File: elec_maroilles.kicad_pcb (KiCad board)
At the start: 2 copper layers, 100 x 90 mm, 88 parts, among them J1 USB_A vert., J2 USB_A vert., J3 Pico5, J4 Dynamixel-3, J5 Dynamixel-3, J6 Pico5, J7 Pico5, J8 Dynamixel-4, J9 Dynamixel-4, Q1 MMBT3906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

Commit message: [update] Positionning v1
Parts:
- removed D3: SP0503BAHT, Package_TO_SOT_SMD:SOT-143
- removed J2: USB_A vert., Library_Pollen:Amphenol_LUSBA11100
- removed TP2, TP4: TestPoint, TestPoint:TestPoint_Pad_D1.0mm
- added J10: PicoBlade 5, Connector_Molex:Molex_PicoBlade_53398-0571_1x05-1MP_P1.25mm_Vertical, F.Cu at (176.6, 63.5)
- added J11: PicoBlade 5, Connector_Molex:Molex_PicoBlade_53398-0571_1x05-1MP_P1.25mm_Vertical, F.Cu at (176.6, 70.5)
- added J12: PicoBlade 5, Connector_Molex:Molex_PicoBlade_53398-0571_1x05-1MP_P1.25mm_Vertical, F.Cu at (176.6, 77.5)
- added R23: DNP - 0R, Resistor_SMD:R_0402_1005Metric, F.Cu at (138.0, 75.8)
- added R24: DNP - 0R, Resistor_SMD:R_0402_1005Metric, F.Cu at (195.9, 62.7)
- added R25: 0R, Resistor_SMD:R_0402_1005Metric, F.Cu at (196.8, 60.9)
- D11, D13, D14, D9: value B5819WS -> DNP - B5819WS
- J4, J5: value Dynamixel-3 -> DNP - Dynamixel-3
- J8, J9: value Dynamixel-4 -> DNP - Dynamixel-4
- moved FID3 117.1 mm to (226.8, 69.4)
- moved H7 83.1 mm to (226.8, 78.4)
- moved J7 81.1 mm to (128.4, 61.1), turned to 180 degrees
- moved D14 74.8 mm to (129.2, 65.8), turned to 90 degrees
- moved D13 73.9 mm to (126.2, 65.8), turned to 90 degrees
- moved FID1 71.6 mm to (89.8, 59.4)
- moved J6 68.4 mm to (214.9, 62.3), turned to 180 degrees
- moved D15 67.4 mm to (214.5, 67.2), turned to -90 degrees
- moved D16 63.2 mm to (211.5, 67.2), turned to -90 degrees
- moved H3 61.7 mm to (99.4, 59.5)
- moved H2 61.2 mm to (92.2, 61.3)
- moved H6 54.4 mm to (226.8, 61.4)
- moved J8 51.5 mm to (155.2, 78.1)
- moved J9 51.5 mm to (161.0, 78.1)
- moved C11 50.5 mm to (133.1, 66.2)
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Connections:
- Q1 pad 3: /Dynamixel TTL/Dynamixel_dir -> Net-(Q1-C)
- Q2 pad 3: /Dynamixel RS485/Dynamixel_dir -> Net-(Q2-C)
- R12 pad 2: /Dynamixel TTL/Dynamixel_dir -> Net-(Q1-C)
- R18 pad 2: /Dynamixel RS485/Dynamixel_dir -> Net-(Q2-C)
- R19 pad 1: /Dynamixel RS485/Dynamixel_dir -> Net-(Q2-C)
- R19 pad 2: Net-(U7-DE) -> /Dynamixel RS485/Dynamixel_dir
- U1 pad 12: /Dynamixel TTL/USB_DynM -> /Dynamixel TTL/USB_DynP
- U3 pad 7: /Dynamixel TTL/USB_DynM -> /Dynamixel TTL/USB_DynP
- U7 pad 2: Net-(U7-DE) -> /Dynamixel RS485/Dynamixel_dir
- U7 pad 3: Net-(U7-DE) -> /Dynamixel RS485/Dynamixel_dir
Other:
- board size 100 x 90 mm -> 150 x 25 mm

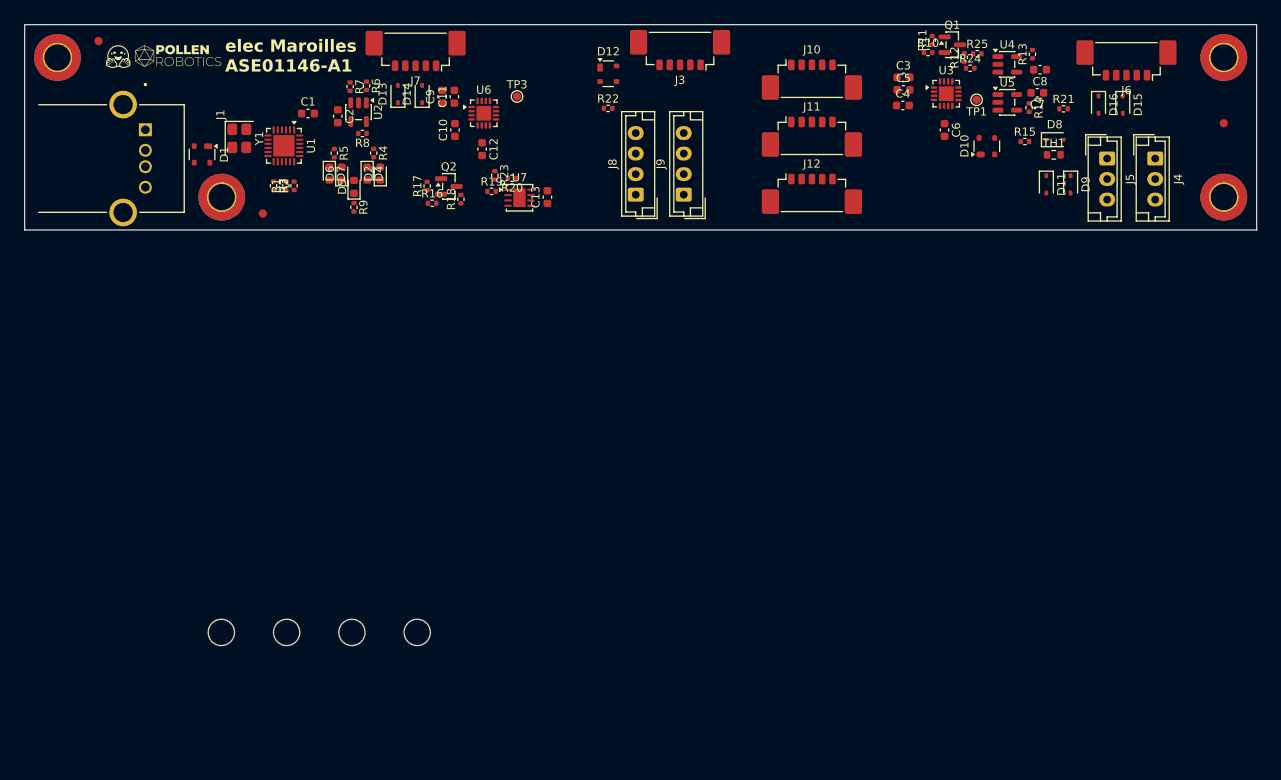
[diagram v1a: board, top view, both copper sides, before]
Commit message: [update] Better positionning.
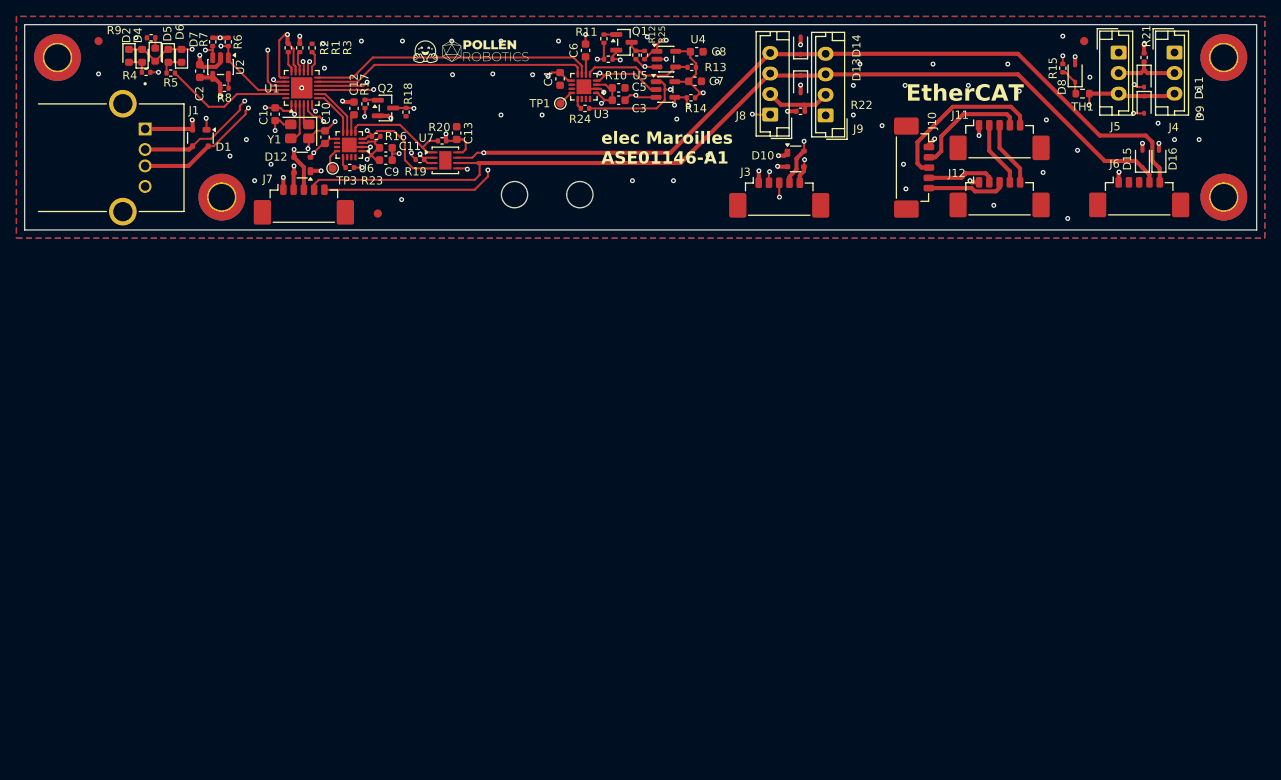
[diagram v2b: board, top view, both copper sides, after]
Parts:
- removed H12, H13: MountingHole_Pad, MountingHole:MountingHole_3.2mm_M3
- moved H10 64.2 mm to (140.4, 78.1)
- moved H11 64.2 mm to (148.4, 78.1)
- moved TP1 50.7 mm to (146.0, 67.0), turned to 0 degrees
- moved D13 49.0 mm to (175.3, 64.7), turned to -90 degrees
- moved R24 47.2 mm to (149.0, 67.6)
- moved D14 46.5 mm to (175.3, 60.0)
- moved C6 44.8 mm to (149.1, 60.5), turned to 90 degrees
- moved U3 44.1 mm to (148.9, 65.0), turned to 180 degrees
- moved C4 41.9 mm to (146.0, 64.0), turned to 90 degrees
- moved C8 41.9 mm to (162.6, 60.7)
- moved C7 41.7 mm to (162.4, 64.3)
- moved U5 41.6 mm to (158.8, 65.3)
- moved U4 41.5 mm to (158.9, 61.6)
- moved R13 41.5 mm to (162.0, 62.6), turned to 180 degrees
- moved R14 41.2 mm to (161.9, 66.3), turned to 180 degrees
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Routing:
- net VBUS: track 0.00 -> 251.5 mm, vias 0 -> 15
- net Net-(D14-K): track 0.00 -> 123.4 mm, vias 0 -> 2
- net Net-(D13-K): track 0.00 -> 117.8 mm
- net /Dynamixel TTL/USB_headP: track 0.00 -> 68.3 mm, vias 0 -> 2
- net /Dynamixel TTL/USB_headM: track 0.00 -> 65.9 mm, vias 0 -> 2
- net Net-(R14-Pad2): track 0.00 -> 63.7 mm, vias 0 -> 4
- net Net-(D9-K): track 0.00 -> 55.7 mm, vias 0 -> 2
- net GND: track 0.00 -> 55.2 mm, vias 0 -> 80
- net /Dynamixel TTL/USB_DynP: track 0.00 -> 34.7 mm
- net /Dynamixel TTL/USB_DynM: track 0.00 -> 33.5 mm
- net /USB hub/DM-: track 0.00 -> 28.0 mm, vias 0 -> 2
- net /USB hub/DM+: track 0.00 -> 26.9 mm, vias 0 -> 2
- net Net-(D2-K): track 0.00 -> 25.4 mm, vias 0 -> 2
- net /Dynamixel TTL/Dynamixel_dir: track 0.00 -> 23.9 mm, vias 0 -> 2
- net Net-(U1-LED1/EESCL): track 0.00 -> 21.7 mm, vias 0 -> 2
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- added copper zone on B.Cu, net GND
- added copper zone on F.Cu, net GND
- added copper zone on In1.Cu, net GND
- added copper zone on In2.Cu, net GND
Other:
- copper layers 2 -> 4
- board text added: "1 mm PCB thickness"
- board text added: "EtherCAT"
- board text added: "top -------- signals in1 -------- gnd + signals //// CORE //// in2 -------- gnd + power bot -------- signals"

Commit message: [update] Release A1 -> in production at JLCPCB qtty 5
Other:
- board text added: "Head"
- board text added: "Left gripper"
- board text added: "Right gripper"
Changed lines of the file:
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@@
 	(title_block
 		(title "carte elec_maroilles")
-		(date "2025-11-26")
+		(date "2025-12-02")
 		(rev "A1")
 		(company "Pollen Robotics / Hugging Face")
@@
 		(tags "connector Molex PicoBlade vertical")
 		(property "Reference" "J12"
-			(at -5.2 -2.35 0)
+			(at -15.601 -3.951 0)
 			(layer "F.SilkS")
 			(effects
@@
 		(tags "connector Molex PicoBlade vertical")
 		(property "Reference" "J10"
-			(at -5.7 -1.65 90)
+			(at -1.601 7.851 90)
 			(layer "F.SilkS")
 			(effects
@@
 		(tags "LED")
 		(property "Reference" "D2"
-			(at -2.5 0.3 90)
+			(at -2.5 0.2 90)
 			(layer "F.SilkS")
 			(effects
@@
 			)
 		)
-		(property "FT Rotation Offset" "180"
+		(property "FT Rotation Offset" ""
 			(at 0 0 270)
 			(unlocked yes)
@@
 			)
 		)
-		(property "FT Rotation Offset" ""
+		(property "FT Rotation Offset" "180"
 			(at 0 0 90)
 			(unlocked yes)
@@
 		(tags "LED")
 		(property "Reference" "D5"
-			(at -2.555 -1.5 90)
+			(at -2.455 -1.7 90)
 			(layer "F.SilkS")
 			(effects
@@
 			)
 		)
-		(property "FT Rotation Offset" ""
+		(property "FT Rotation Offset" "180"
 			(at 0 0 270)
 			(unlocked yes)
@@
 			)
 		)
-		(property "FT Rotation Offset" ""
+		(property "FT Rotation Offset" "180"
 			(at 0 0 90)
 			(unlocked yes)
@@
 		(tags "LED")
 		(property "Reference" "D6"
-			(at -2.9 -1.4 90)
+			(at -2.6 -1.6 90)
 			(layer "F.SilkS")
 			(effects
@@
 			)
 		)
-		(property "FT Rotation Offset" "180"
+		(property "FT Rotation Offset" ""
 			(at 0 0 270)
 			(unlocked yes)
@@
 		(tags "connector Molex PicoBlade vertical")
 		(property "Reference" "J11"
-			(at -4.8 -2.5 0)
+			(at -15.601 1.599 0)
 			(layer "F.SilkS")
 			(effects
@@
 		)
 	)
+	(gr_text "Left\ngripper"
+		(at 225.1775 74.4 0)
+		(layer "F.SilkS" knockout)
+		(effects
+			(font
+				(size 1.2 1.2)
+				(thickness 0.24)
+				(bold yes)
+			)
+			(justify bottom)
+		)
+	)
 	(gr_text "elec Maroilles\nASE01146-A1"
 		(at 150.9775 74.5 0)
@@
 		)
 	)
+	(gr_text "Right gripper"
+		(at 124.9775 81.3 0)
+		(layer "F.SilkS" knockout)
+		(effects
+			(font
+				(size 1.2 1.2)
+				(thickness 0.24)
+				(bold yes)
+			)
+			(justify left bottom)
+		)
+	)
+	(gr_text "Head"
+		(at 177.4775 76.7 0)
+		(layer "F.SilkS" knockout)
+		(effects
+			(font
+				(size 1.2 1.2)
+				(thickness 0.24)
+				(bold yes)
+			)
+			(justify left bottom)
+		)
+	)
 	(gr_text "EtherCAT"
 		(at 188.0775 66.9 0)
@@
 			)
 		)
+	)
+	(zone
+		(net 0)
+		(net_name "")
+		(layer "F.SilkS")
+		(hatch full 0.5)
+		(connect_pads
+			(clearance 0.5)
+		)
+		(min_thickness 0.25)
+		(filled_areas_thickness no)
+		(fill yes
+			(thermal_gap 0.5)
+			(thermal_bridge_width 0.5)
+		)
+		(polygon
+			(pts
+				(xy 188.4775 64.3) (xy 185.5775 68) (xy 185.5775 81.9) (xy 206.5775 81.9) (xy 206.5775 69.4) (xy 201.3775 64.3)
+			)
+		)

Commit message: [update] Release B1!
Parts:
- moved TP3 2.77 mm to (120.4, 76.7)
- moved D12 1.90 mm to (116.5, 74.6)
- moved D15 1.90 mm to (215.0, 73.8)
- moved D16 1.90 mm to (217.0, 73.8)
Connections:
- D13 pad 1: Net-(D13-K) -> /Dynamixel RS485/DynD+
- D14 pad 1: Net-(D14-K) -> /Dynamixel RS485/DynD-
- D15 pad 1: Net-(D13-K) -> /Dynamixel RS485/DynD+
- D16 pad 1: Net-(D14-K) -> /Dynamixel RS485/DynD-
- J6 pad 2: unconnected-(J6-Pin_2-Pad2) -> /Dynamixel RS485/DynD+
- J6 pad 3: unconnected-(J6-Pin_3-Pad3) -> /Dynamixel RS485/DynD-
- J6 pad 4: Net-(D13-K) -> unconnected-(J6-Pin_4-Pad4)
- J6 pad 5: Net-(D14-K) -> unconnected-(J6-Pin_5-Pad5)
- J7 pad 2: /Dynamixel RS485/USB_gripperP -> /Dynamixel RS485/DynD+
- J7 pad 3: /Dynamixel RS485/USB_gripperM -> /Dynamixel RS485/DynD-
- J7 pad 4: Net-(D13-K) -> /Dynamixel RS485/USB_gripperP
- J7 pad 5: Net-(D14-K) -> /Dynamixel RS485/USB_gripperM
- J8 pad 3: Net-(D13-K) -> /Dynamixel RS485/DynD+
- J8 pad 4: Net-(D14-K) -> /Dynamixel RS485/DynD-
- J9 pad 3: Net-(D13-K) -> /Dynamixel RS485/DynD+
- J9 pad 4: Net-(D14-K) -> /Dynamixel RS485/DynD-
- U7 pad 6: Net-(D13-K) -> /Dynamixel RS485/DynD+
- U7 pad 7: Net-(D14-K) -> /Dynamixel RS485/DynD-
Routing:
- net /Dynamixel RS485/DynD-: track 0.00 -> 126.6 mm, vias 0 -> 2
- net Net-(D14-K): track 123.4 -> 0.00 mm, vias 2 -> 0
- net /Dynamixel RS485/DynD+: track 0.00 -> 118.9 mm, vias 0 -> 2
- net Net-(D13-K): track 117.8 -> 0.00 mm
- net Net-(U6-~{DTR}): track 2.67 -> 4.72 mm
- net /Dynamixel RS485/USB_gripperP: track 12.5 -> 13.4 mm
- net GND: track 55.2 -> 56.1 mm
- net /Dynamixel RS485/USB_gripperM: track 14.0 -> 14.8 mm
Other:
- board text added: "Gripper"
- board text added: "elec Maroilles ASE01146-B1"
- board text removed: "Left gripper"
- board text removed: "Right gripper"
- board text removed: "elec Maroilles ASE01146-A1"
